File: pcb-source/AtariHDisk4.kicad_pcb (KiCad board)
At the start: 4 copper layers, 97.3 x 69.6 mm, 78 parts, among them J1 JTAG, J10 ST ACSI BUS, J14 MicroSD Card 0, J2 Program_enable, J3 SD Card 1, J4 UPDI, J5 Conn_01x02_Female, J6 Conn_02x03_Odd_Even, Q3 BC847, Q4 BC847, U1 74LVC245, U11 74LVC8T245, U2 MAX3232, U3 AZ1117-5.0, U4 Oscillator7x5, U5 MCP795xx, U7 AMS1117-3.3, U8 AMS1117-1.8, U9 5M80Z, Y1 32KHz

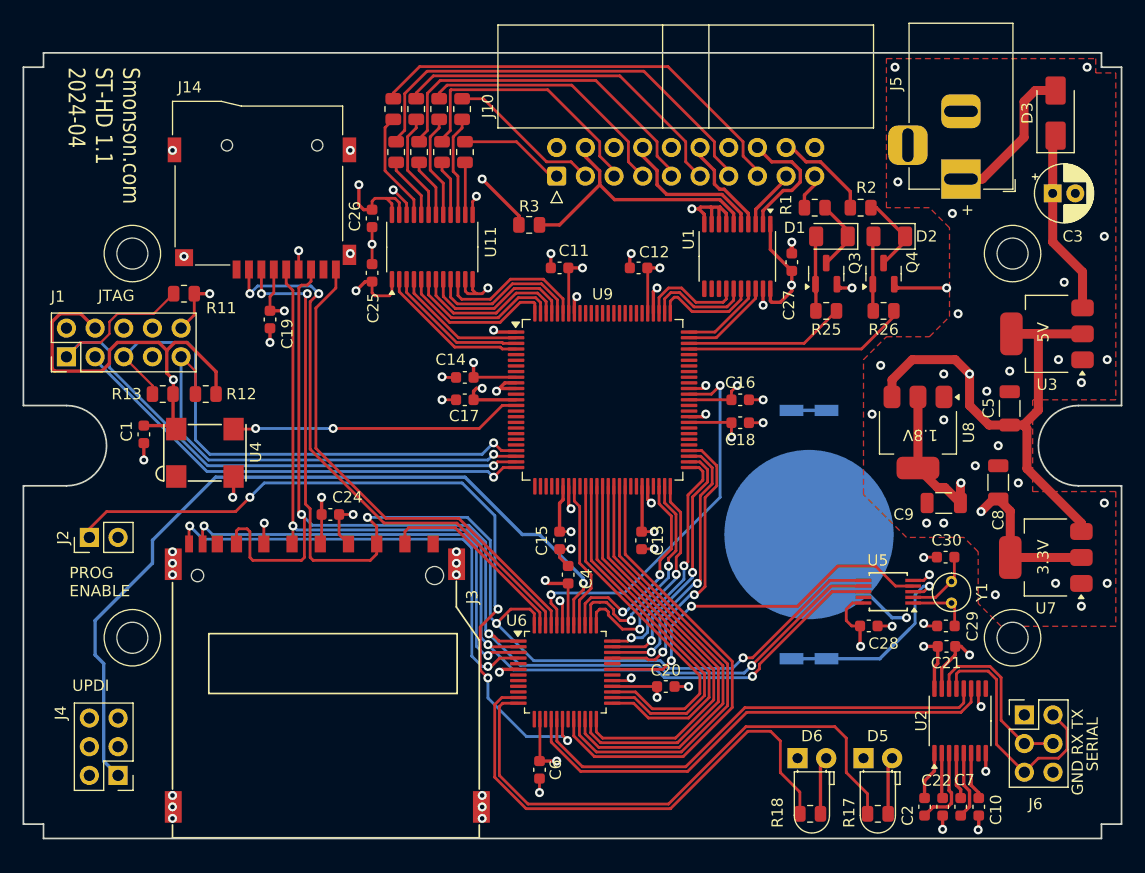
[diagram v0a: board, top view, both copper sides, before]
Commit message: Switched the avr128da to an stm32c031
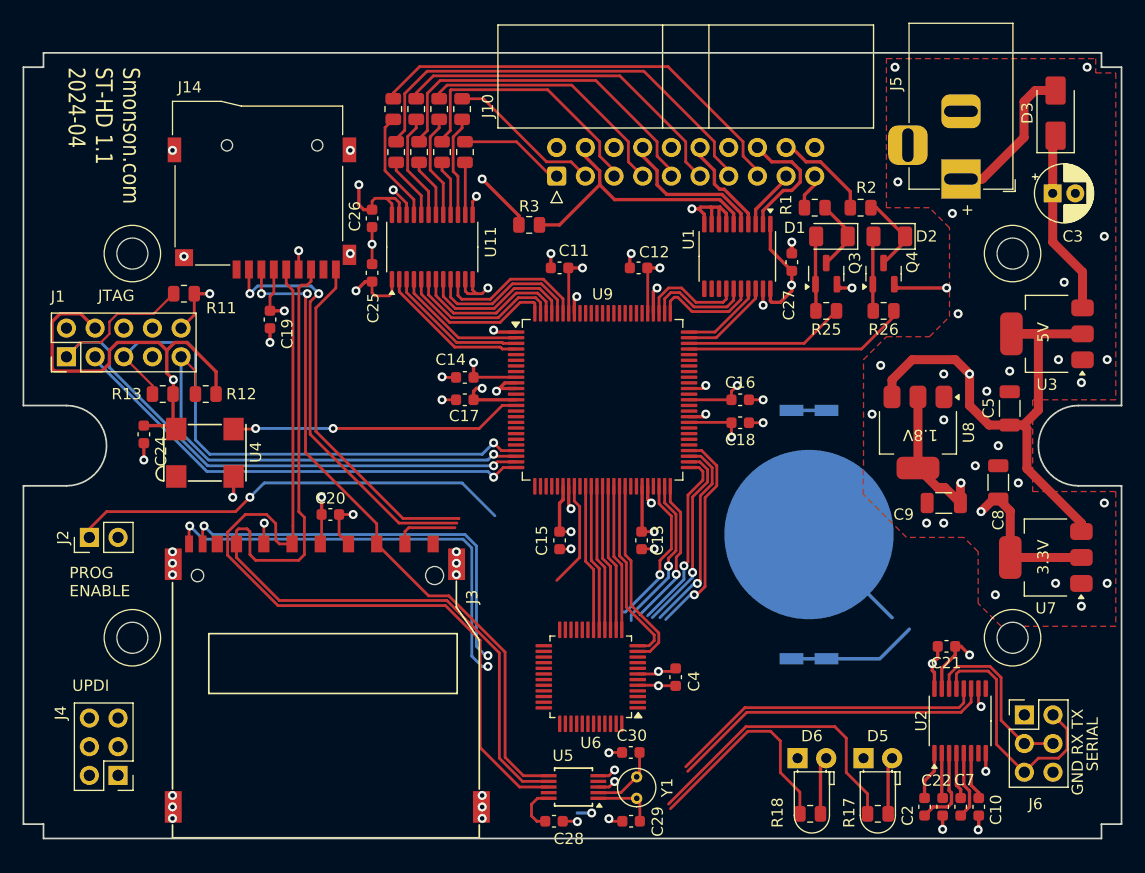
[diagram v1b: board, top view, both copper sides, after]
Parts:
- removed C1, C6: 0.1uF, Capacitor_SMD:C_0603_1608Metric
- C21, C28: value C -> 0.1uF
- R17, R18: value 2K -> 220
- R25, R26: value R -> 1K
- U6: value ~ -> STM32C031CxT
- moved C20 33.4 mm to (82.1, 100.1)
- moved C30 32.8 mm to (108.7, 121.2)
- moved C28 32.8 mm to (101.9, 127.3)
- moved C29 32.8 mm to (108.7, 127.3)
- moved Y1 32.8 mm to (109.2, 123.3)
- moved U5 32.8 mm to (103.6, 124.2)
- moved C24 18.0 mm to (65.5, 93.0), turned to -90 degrees
- moved C4 13.2 mm to (112.6, 114.5)
- moved U6 2.29 mm to (105.1, 114.5), turned to 180 degrees
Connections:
- J2 pad 1: Net-(J2-Pin_1) -> unconnected-(J2-Pin_1-Pad1)
- J4 pad 1: /ATMega/UPDI -> /Microcontroller/UPDI
- R17 pad 1: /ATMega/LED0 -> /Microcontroller/LED0
- R18 pad 1: /ATMega/LED1 -> /Microcontroller/LED1
- U2 pad 11: /ATMega/TX -> /Microcontroller/TX
- U2 pad 12: /ATMega/RX -> /Microcontroller/RX
- U5 pad 4: /ATMega/CLK_SS -> /Microcontroller/CLK_SS
- U6 pad 1: /MISO -> unconnected-(U6-PC13-Pad1)
- U6 pad 11: /ATMega/LED1 -> /A_D0
- U6 pad 12: /ATMega/LED0 -> /A_D1
- U6 pad 13: unconnected-(U6-PC3-Pad13) -> /A_D2
- U6 pad 14: +3V3 -> /A_D3
- U6 pad 15: (no net) -> /A_D4
- U6 pad 16: /ATMega/TX -> /A_D5
- U6 pad 17: /ATMega/RX -> /A_D6
- U6 pad 18: Net-(J2-Pin_1) -> /A_D7
- U6 pad 2: /SCK -> unconnected-(U6-PC14-Pad2)
- U6 pad 20: /A_D0 -> unconnected-(U6-PB1-Pad20)
- U6 pad 21: /A_D1 -> unconnected-(U6-PB2-Pad21)
- U6 pad 22: /A_D2 -> unconnected-(U6-PB10-Pad22)
- U6 pad 23: /A_D3 -> unconnected-(U6-PB11-Pad23)
- U6 pad 24: /A_D4 -> unconnected-(U6-PB12-Pad24)
- U6 pad 25: /A_D5 -> unconnected-(U6-PB13-Pad25)
- U6 pad 26: /A_D6 -> unconnected-(U6-PB14-Pad26)
- U6 pad 27: /A_D7 -> unconnected-(U6-PB15-Pad27)
- U6 pad 28: +3V3 -> unconnected-(U6-PA8-Pad28)
- U6 pad 29: GND -> unconnected-(U6-PA9-Pad29)
- U6 pad 3: /CARD1_DET -> unconnected-(U6-PC15-Pad3)
- U6 pad 31: /ATMega/CLK_SS -> unconnected-(U6-PC7-Pad31)
- U6 pad 33: /A_EXTRA2 -> unconnected-(U6-PA11-Pad33)
- U6 pad 34: /A_EXTRA -> unconnected-(U6-PA12-Pad34)
- U6 pad 35: /A_READY -> unconnected-(U6-SWDIO-Pad35)
- U6 pad 36: /A_INT -> unconnected-(U6-SWCLK-Pad36)
- U6 pad 37: /A_CMD -> unconnected-(U6-PA15-Pad37)
- U6 pad 38: /A_BUS_DIR -> unconnected-(U6-PD0-Pad38)
- U6 pad 39: /A_CS -> unconnected-(U6-PD1-Pad39)
- U6 pad 4: /CARD1_WP -> unconnected-(U6-PF3-Pad4)
- U6 pad 40: /A_RESET -> unconnected-(U6-PD2-Pad40)
- U6 pad 41: /ATMega/UPDI -> (no net)
- U6 pad 42: +3V3 -> /SCK
- U6 pad 43: GND -> /MISO
- U6 pad 44: /CLOCK8 -> /MOSI
- U6 pad 45: /CARD0_DET -> unconnected-(U6-PB6-Pad45)
- U6 pad 46: /AVR_SS0 -> unconnected-(U6-PB7-Pad46)
- U6 pad 47: /AVR_SS1 -> unconnected-(U6-PB8-Pad47)
- U6 pad 48: /MOSI -> unconnected-(U6-PB9-Pad48)
- U6 pad 5: unconnected-(U6-PB1-Pad5) -> +3V3
- U6 pad 6: GND -> +3V3
- U6 pad 7: unconnected-(U6-PB3-Pad7) -> GND
- U9 pad 64: /CLOCK8 -> unconnected-(U9-IO/CLK3-Pad64)
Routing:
- net +3V3: track 449.2 -> 272.3 mm, vias 17 -> 14
- net /ATMega/UPDI: track 72.5 -> 0.00 mm, vias 1 -> 0
- net Net-(J2-Pin_1): track 67.5 -> 0.00 mm, vias 4 -> 0
- net /ATMega/LED0: track 50.4 -> 0.00 mm
- net /ATMega/LED1: track 45.6 -> 0.00 mm
- net /ATMega/TX: track 44.0 -> 0.00 mm
- net /ATMega/RX: track 42.6 -> 0.00 mm
- net /MOSI: track 101.4 -> 60.3 mm, vias 5 -> 2
- net unconnected-(J2-Pin_1-Pad1): track 0.00 -> 39.6 mm, vias 0 -> 1
- net /CLOCK8: track 34.5 -> 0.00 mm, vias 2 -> 0
- net /ATMega/CLK_SS: track 33.0 -> 0.00 mm, vias 2 -> 0
- net /Microcontroller/TX: track 0.00 -> 28.9 mm
- net /Microcontroller/RX: track 0.00 -> 28.2 mm
- net /Microcontroller/LED0: track 0.00 -> 26.5 mm
- net /A_D2: track 38.9 -> 13.0 mm
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- added copper zone on In2.Cu, net +3V3

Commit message: Final board setup that was sent to production
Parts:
- removed J4: UPDI, Connector_PinHeader_2.54mm:PinHeader_2x03_P2.54mm_Vertical
- added J7: ST-LINK, Connector_PinHeader_2.54mm:PinHeader_2x05_P2.54mm_Vertical, F.Cu at (63.3, 125.5)
- added JP1: SolderJumper_2_Open, Jumper:SolderJumper-2_P1.3mm_Open_RoundedPad1.0x1.5mm, F.Cu at (94.2, 95.9)
- Y1: footprint Crystal:Crystal_C38-LF_D3.0mm_L8.0mm_Vertical -> simon:Crystal_SMD_ECX_31B-2Pin_3.2x1.5mm
- moved C24 25.6 mm to (90.2, 86.1), turned to 180 degrees
- moved U4 18.0 mm to (88.8, 91.8), turned to 90 degrees
- moved C27 6.04 mm to (120.6, 83.3), turned to 180 degrees
- moved BT1 5.71 mm to (125.2, 107.5)
- moved C25 4.31 mm to (87.6, 82.5), turned to 0 degrees
- moved C30 2.99 mm to (111.3, 122.7), turned to 90 degrees
- moved C29 2.97 mm to (111.3, 125.7), turned to -90 degrees
- moved C26 2.18 mm to (84.8, 71.9), turned to 90 degrees
- moved C19 2.16 mm to (78.2, 81.3), turned to 0 degrees
- moved U6 1.72 mm to (105.1, 112.7)
- moved C11 1.54 mm to (103.9, 78.2), turned to 0 degrees
- moved C13 1.33 mm to (110.0, 101.1), turned to 0 degrees
- moved C15 1.28 mm to (102.4, 101.1), turned to 0 degrees
- moved C16 1.28 mm to (117.3, 89.1), turned to 90 degrees
- moved C14 1.13 mm to (94.7, 87.1), turned to 90 degrees
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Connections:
- J2 pad 1: unconnected-(J2-Pin_1-Pad1) -> Net-(J2-Pin_1)
- U6 pad 1: unconnected-(U6-PC13-Pad1) -> /Microcontroller/LED1
- U6 pad 10: unconnected-(U6-NRST-Pad10) -> /F_RESET
- U6 pad 19: unconnected-(U6-PB0-Pad19) -> /A_CS
- U6 pad 2: unconnected-(U6-PC14-Pad2) -> /Microcontroller/LED0
- U6 pad 20: unconnected-(U6-PB1-Pad20) -> /A_BUS_DIR
- U6 pad 21: unconnected-(U6-PB2-Pad21) -> /A_CMD
- U6 pad 22: unconnected-(U6-PB10-Pad22) -> /A_EXTRA2
- U6 pad 23: unconnected-(U6-PB11-Pad23) -> /A_EXTRA
- U6 pad 28: unconnected-(U6-PA8-Pad28) -> /A_CLKOUT
- U6 pad 29: unconnected-(U6-PA9-Pad29) -> Net-(J2-Pin_1)
- U6 pad 30: unconnected-(U6-PC6-Pad30) -> /CARD0_DET
- U6 pad 31: unconnected-(U6-PC7-Pad31) -> /AVR_SS0
- U6 pad 32: unconnected-(U6-PA10-Pad32) -> /AVR_SS1
- U6 pad 33: unconnected-(U6-PA11-Pad33) -> /CARD1_DET
- U6 pad 34: unconnected-(U6-PA12-Pad34) -> /CARD1_WP
- U6 pad 35: unconnected-(U6-SWDIO-Pad35) -> /Microcontroller/SWDIO
- U6 pad 36: unconnected-(U6-SWCLK-Pad36) -> /Microcontroller/SWCLK
- U6 pad 40: unconnected-(U6-PD2-Pad40) -> /Microcontroller/CLK_SS
- U6 pad 45: unconnected-(U6-PB6-Pad45) -> /Microcontroller/TX
- U6 pad 46: unconnected-(U6-PB7-Pad46) -> /Microcontroller/RX
- U6 pad 8: unconnected-(U6-PF0-Pad8) -> /A_READY
- U6 pad 9: unconnected-(U6-PF1-Pad9) -> /A_INT
- U9 pad 26: unconnected-(U9-IO-Pad26) -> /A_EXTRA
- U9 pad 27: unconnected-(U9-IO-Pad27) -> /A_EXTRA2
- U9 pad 28: unconnected-(U9-IO-Pad28) -> /A_CMD
- U9 pad 29: unconnected-(U9-IO-Pad29) -> /A_BUS_DIR
- U9 pad 33: /A_RESET -> unconnected-(U9-IO-Pad33)
- U9 pad 34: unconnected-(U9-IO-Pad34) -> /A_CS
- U9 pad 48: /A_CS -> unconnected-(U9-IO-Pad48)
- U9 pad 49: /A_BUS_DIR -> /A_INT
- U9 pad 50: /A_CMD -> /A_READY
- U9 pad 51: /A_INT -> unconnected-(U9-IO-Pad51)
- U9 pad 52: /A_READY -> unconnected-(U9-IO-Pad52)
- U9 pad 53: /A_EXTRA -> unconnected-(U9-IO-Pad53)
- U9 pad 54: /A_EXTRA2 -> unconnected-(U9-IO-Pad54)
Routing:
- net +3V3: track 272.3 -> 109.1 mm, vias 14 -> 16
- net /F_RESET: track 9.27 -> 98.2 mm, vias 0 -> 3
- net Net-(J2-Pin_1): track 0.00 -> 53.0 mm, vias 0 -> 2
- net /Microcontroller/SWDIO: track 0.00 -> 46.2 mm, vias 0 -> 1
- net /Microcontroller/SWCLK: track 0.00 -> 46.0 mm, vias 0 -> 1
- net unconnected-(J2-Pin_1-Pad1): track 39.6 -> 0.00 mm, vias 1 -> 0
- net /Microcontroller/CLK_SS: track 0.00 -> 20.8 mm, vias 0 -> 2
- net /AVR_SS1: track 5.68 -> 25.3 mm
- net /A_CLKOUT: track 0.00 -> 18.4 mm
- net +1V8: track 71.2 -> 89.2 mm
- net /MISO: track 78.6 -> 96.0 mm, vias 0 -> 3
- net /CARD0_DET: track 30.9 -> 47.6 mm
- net /CLK32: track 25.9 -> 10.8 mm, vias 2 -> 0
- net /MOSI: track 60.3 -> 75.0 mm
- net GND: track 106.2 -> 120.0 mm, vias 85 -> 75
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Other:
- board text added: "5M80Z"
- board text added: "74LVC 245"
- board text added: "74LVC 8T245"
- board text added: "CR2016"
- board text added: "G"
- board text added: "MAX 3232"
- board text added: "MCP 79510"
- board text added: "R"
- board text added: "ST-LINK CLONE"
- board text added: "STM32 C031"
- board text removed: "UPDI"
